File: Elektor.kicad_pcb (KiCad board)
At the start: 2 copper layers, 54 parts, among them J1 Conn_Coaxial, J13 Conn_Coaxial, J6 Conn_01x03_Pin, J7 Conn_01x02, J8 Conn_01x02, Q1 BF545B, U1 Si5351A-B-GT, U2 74HC74, U3 74HC4066D_653, U5 MCP6022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

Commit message: routage plus compact
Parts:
- removed J7: Conn_01x02, Connector_PinHeader_2.54mm:PinHeader_1x02_P2.54mm_Vertical
- added C14: 4.7u, Capacitor_THT:C_Rect_L4.0mm_W2.5mm_P2.50mm, F.Cu at (175.5, 64.5)
- added C8: 4.7u, Capacitor_THT:C_Rect_L4.0mm_W2.5mm_P2.50mm, F.Cu at (170.1, 66.0)
- R19: moved to B.Cu
- U2: value 74HC74 -> 74HC04; footprint Package_SO:SO-14_5.3x10.2mm_P1.27mm -> Package_SO:SOIC-14_3.9x8.7mm_P1.27mm
- moved R10 33.7 mm to (186.9, 68.3), turned to 90 degrees
- moved R12 33.2 mm to (183.6, 63.0), turned to 180 degrees
- moved C15 31.3 mm to (178.8, 68.8), turned to -90 degrees
- moved C3 28.4 mm to (184.9, 75.2)
- moved C4 27.5 mm to (185.2, 77.7), turned to 180 degrees
- moved R11 27.2 mm to (187.0, 63.0), turned to 180 degrees
- moved U5 26.3 mm to (182.9, 68.6), turned to 90 degrees
- moved J6 26.1 mm to (170.7, 97.0), turned to 0 degrees
- moved R9 25.8 mm to (186.9, 75.2)
- moved C6 25.4 mm to (180.8, 75.2), turned to 90 degrees
- moved Y1 24.4 mm to (166.1, 98.7), turned to 90 degrees
- moved C17 23.2 mm to (192.0, 68.6), turned to -90 degrees
- moved R3 23.2 mm to (174.8, 99.6), turned to 90 degrees
- moved R13 22.9 mm to (182.9, 75.2)
- moved C5 22.7 mm to (181.6, 77.7), turned to 180 degrees
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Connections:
- C15 pad 1: Net-(U2A-~{R}) -> 5VA
- C15 pad 2: GND -> GNDA
- C16 pad 1: Net-(U2A-~{R}) -> Net-(U2G-VCC)
- R12 pad 2: Net-(R12-Pad2) -> Net-(C8-Pad1)
- R17 pad 2: Net-(R17-Pad2) -> Net-(C14-Pad1)
- R5 pad 1: Net-(U2A-~{R}) -> Net-(U2G-VCC)
- U1 pad 10: Net-(J7-Pin_1) -> Net-(U1-CLK0)
- U2 pad 1: Net-(U2A-~{R}) -> Net-(U1-CLK0)
- U2 pad 10: Net-(U2A-~{R}) -> unconnected-(U2-Pad10)
- U2 pad 11: Net-(U1-CLK1) -> Net-(U2G-VCC)
- U2 pad 12: Net-(U2A-~{Q}) -> unconnected-(U2-Pad12)
- U2 pad 13: Net-(U2A-~{R}) -> Net-(U2G-VCC)
- U2 pad 14: Net-(U2A-~{R}) -> Net-(U2G-VCC)
- U2 pad 2: Net-(U2A-D) -> Net-(U3-1E)
- U2 pad 4: Net-(U2A-~{R}) -> Net-(U3-4E)
- U2 pad 5: Net-(U2A-Q) -> Net-(U2G-VCC)
- U2 pad 6: Net-(U2A-~{Q}) -> unconnected-(U2-Pad6)
- U2 pad 8: Net-(U2B-~{Q}) -> unconnected-(U2-Pad8)
- U2 pad 9: Net-(U2A-D) -> Net-(U2G-VCC)
- U3 pad 12: Net-(U2A-~{Q}) -> Net-(U3-4E)
- U3 pad 13: Net-(U2B-~{Q}) -> Net-(U3-1E)
- U3 pad 14: Net-(U2A-~{R}) -> Net-(U2G-VCC)
- U3 pad 5: Net-(U2A-D) -> Net-(U1-CLK0)
- U3 pad 6: Net-(U2A-Q) -> Net-(U1-CLK1)
- U5 pad 7: Net-(R12-Pad2) -> Net-(C8-Pad1)
- U6 pad 5V: Net-(U2A-~{R}) -> Net-(U2G-VCC)
- U6 pad INL: Net-(R12-Pad2) -> Net-(C8-Pad2)
- U6 pad INR: Net-(R17-Pad2) -> Net-(C14-Pad2)
- U7 pad 7: Net-(R17-Pad2) -> Net-(C14-Pad1)
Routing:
- net Net-(U2A-~{R}): track 89.3 -> 0.00 mm, vias 6 -> 0
- net GND: track 174.0 -> 115.5 mm, vias 9 -> 8
- net Net-(U3-2Z): track 64.6 -> 16.4 mm, vias 4 -> 2
- net Net-(U2A-D): track 47.2 -> 0.00 mm, vias 4 -> 0
- net Net-(U2G-VCC): track 0.00 -> 42.6 mm, vias 0 -> 2
- net Net-(U2A-~{Q}): track 40.8 -> 0.00 mm, vias 4 -> 0
- net Net-(U3-1Z): track 56.7 -> 20.1 mm, vias 4 -> 2
- net Net-(U2B-~{Q}): track 33.2 -> 0.00 mm, vias 2 -> 0
- net Net-(U2A-Q): track 27.2 -> 0.00 mm, vias 5 -> 0
- net Net-(C14-Pad1): track 0.00 -> 26.6 mm, vias 0 -> 3
- net Net-(U1-CLK0): track 0.00 -> 26.5 mm, vias 0 -> 2
- net Net-(R12-Pad2): track 25.5 -> 0.00 mm, vias 2 -> 0
- net Net-(U3-4E): track 0.00 -> 21.2 mm
- net Net-(U3-1E): track 0.00 -> 20.6 mm
- net Net-(J6-Pin_3): track 4.88 -> 25.0 mm
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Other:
- board outline added: 53 x 44 mm

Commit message: avec plan de masse
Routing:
- net GND: track 115.5 -> 136.0 mm, vias 8 -> 11
- net Net-(U3-4E): track 21.2 -> 19.7 mm
- net Net-(U6-SCL): vias 3 -> 2
- net 3.3V: vias 11 -> 10
- added copper zone on B.Cu, net GND
- added copper zone on B.Cu, net GNDA
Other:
- board size 53 x 44 mm -> 53 x 44.1 mm

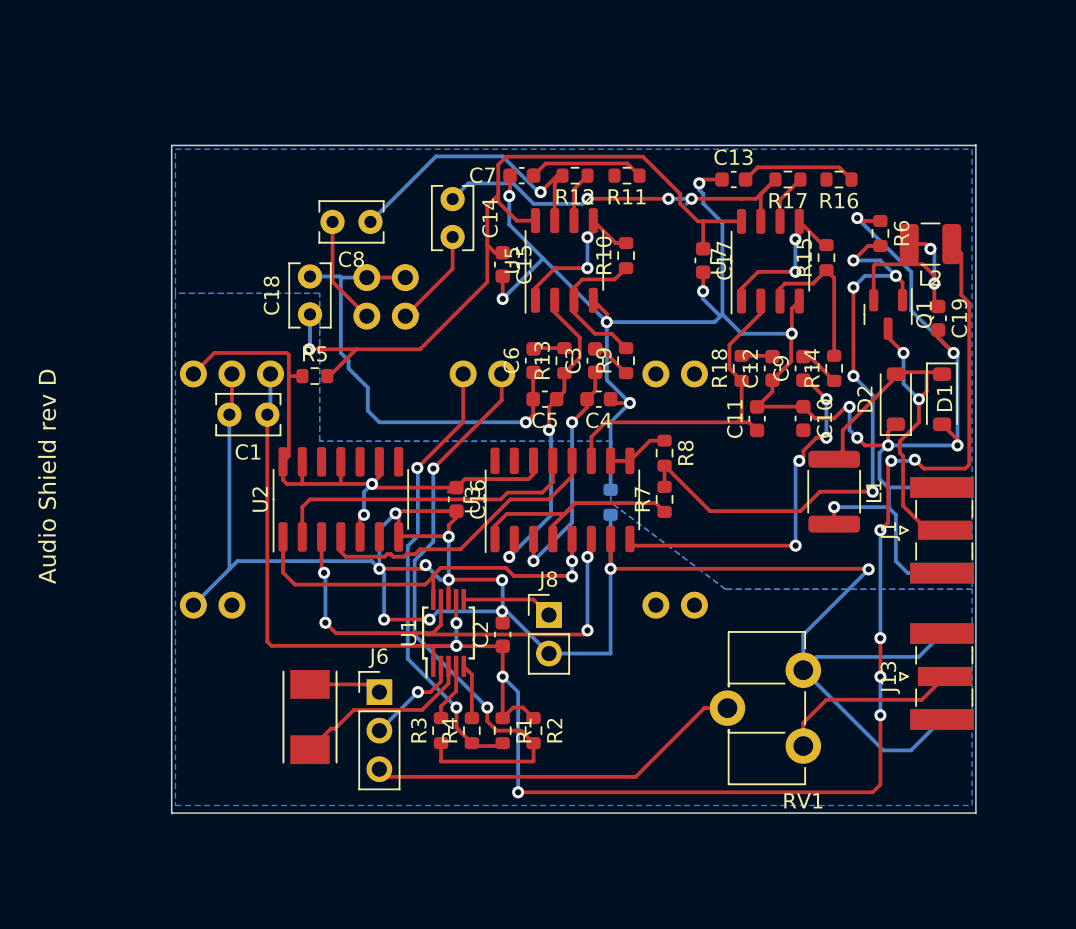
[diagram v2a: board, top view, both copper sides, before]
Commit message: meilleur plan de masse
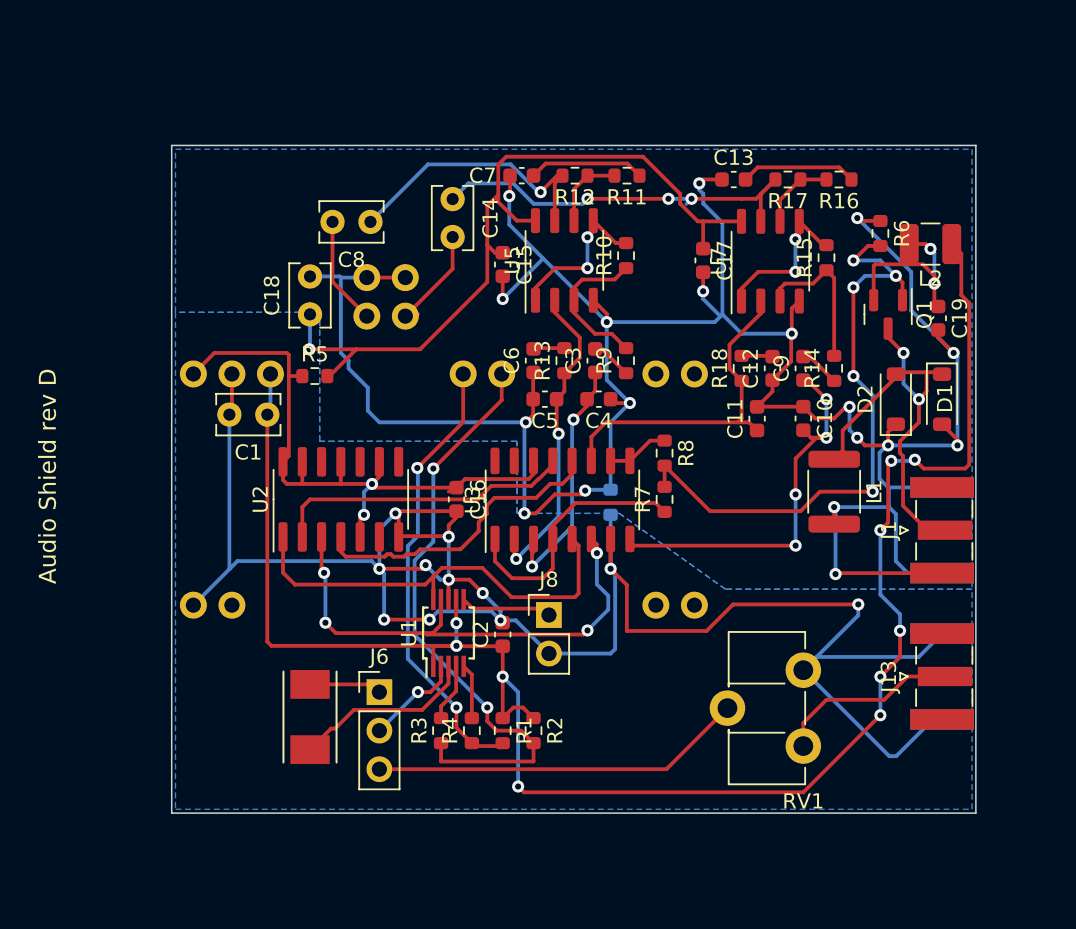
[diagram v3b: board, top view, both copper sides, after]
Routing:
- net GNDA: track 161.5 -> 183.6 mm, vias 15 -> 18
- net Net-(U1-CLK0): track 26.5 -> 28.8 mm, vias 2 -> 0
- net 3.3V: track 121.6 -> 119.7 mm
- net Net-(U5B--): track 3.33 -> 5.11 mm
- net Net-(U3-3Y): track 24.1 -> 25.9 mm
- net Net-(U7B--): track 3.31 -> 5.03 mm
- net Net-(U3-2Z): track 16.4 -> 18.0 mm
- net Net-(U3-1Y): track 15.6 -> 17.1 mm
- net Net-(U3-1Z): track 19.6 -> 20.9 mm
- net Net-(U1-CLK1): track 32.5 -> 33.4 mm
- net Net-(U3-1E): track 20.6 -> 19.9 mm
- net Net-(U3-4E): track 19.7 -> 20.3 mm
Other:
- board size 53 x 44.1 mm -> 53 x 44 mm

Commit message: plus compact
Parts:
- moved R1 22.7 mm to (169.9, 78.7), turned to 90 degrees
- moved R2 22.1 mm to (173.8, 78.7), turned to 90 degrees
- moved R6 22.0 mm to (193.0, 86.1), turned to 90 degrees
- moved L2 21.6 mm to (199.5, 87.8), turned to 90 degrees
- moved R4 21.4 mm to (171.8, 78.8), turned to -90 degrees
- moved Re 20.6 mm to (175.5, 79.0), turned to -90 degrees
- moved C19 19.3 mm to (195.5, 87.5), turned to 180 degrees
- moved Q1 14.5 mm to (195.8, 83.9), turned to 90 degrees
- moved J8 12.0 mm to (172.5, 99.5), turned to 90 degrees
- moved J1 9.52 mm to (205.0, 77.2)
- moved D1 8.47 mm to (205.8, 69.5), turned to 90 degrees
- moved D2 8.40 mm to (203.0, 69.5), turned to -90 degrees
- moved RV1 8.31 mm to (193.2, 94.2), turned to -90 degrees
- moved Y1 6.40 mm to (170.8, 94.2), turned to -90 degrees
- moved J6 5.64 mm to (166.5, 93.2)
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- renumbered R3 to Re
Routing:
- net GND: track 136.2 -> 96.6 mm, vias 11 -> 6
- net 3.3V: track 119.7 -> 84.4 mm, vias 10 -> 1
- net Net-(Q1-S): track 41.5 -> 7.59 mm, vias 5 -> 0
- net Net-(U6-SDA): track 39.4 -> 6.01 mm, vias 2 -> 0
- net Net-(U6-SCL): track 30.6 -> 7.89 mm, vias 2 -> 0
- net Net-(U3-3Y): track 25.9 -> 7.55 mm, vias 4 -> 2
- net Net-(U1-SDA): track 3.63 -> 13.4 mm, vias 0 -> 2
- net Net-(U1-SCL): track 3.82 -> 13.6 mm, vias 0 -> 2
- net Net-(Q1-D): track 13.2 -> 6.21 mm, vias 2 -> 0
- net Net-(U1-XB): track 12.9 -> 6.56 mm
- net GNDA: track 183.6 -> 177.8 mm, vias 18 -> 13
- net Net-(J6-Pin_3): track 24.6 -> 30.4 mm, vias 0 -> 1
- net Net-(J6-Pin_2): track 6.40 -> 11.0 mm, vias 1 -> 0
- net Net-(D1-K): track 29.0 -> 25.4 mm, vias 2 -> 0
- net Net-(U1-CLK0): track 28.8 -> 31.9 mm, vias 0 -> 4
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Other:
- board size 53 x 44 mm -> 50 x 44 mm

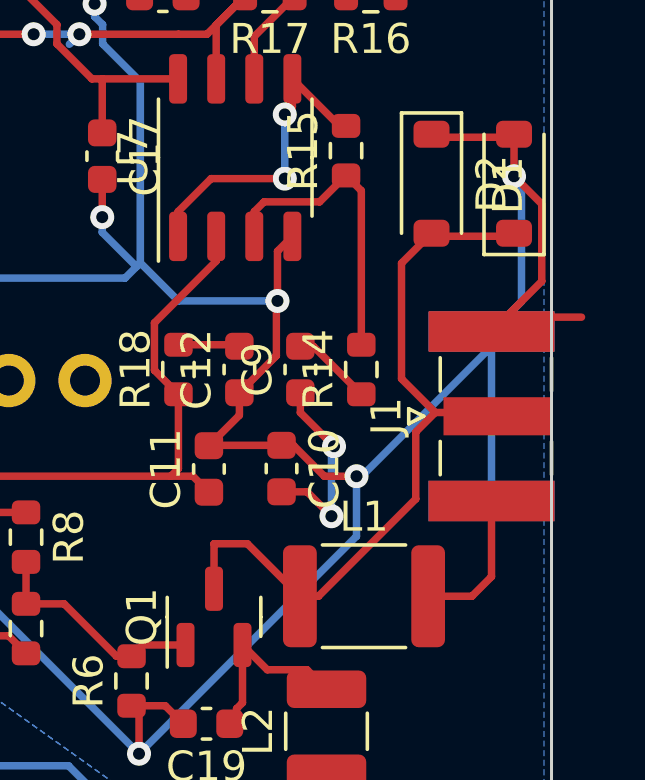
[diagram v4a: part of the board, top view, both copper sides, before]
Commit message: ajout connexion manquante
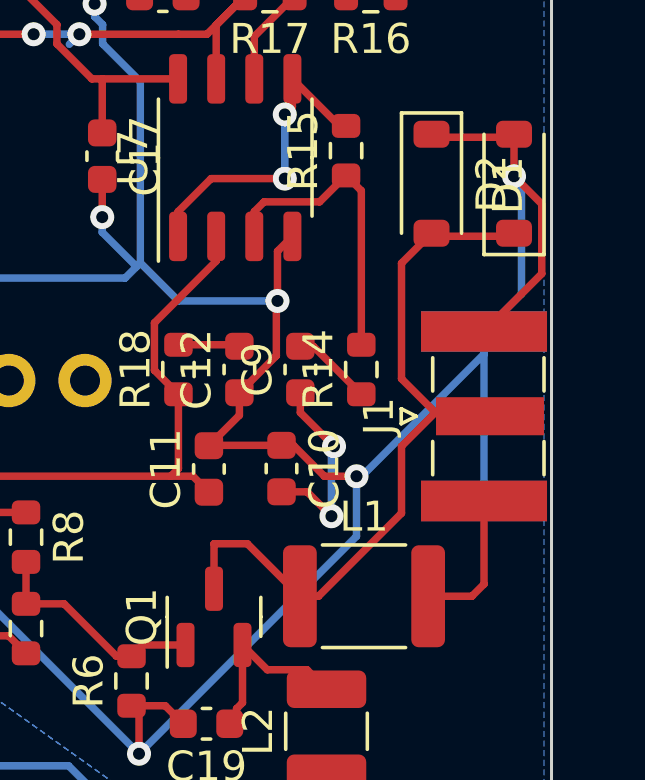
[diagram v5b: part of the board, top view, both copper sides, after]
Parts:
- moved J1 0.25 mm to (204.8, 77.2)
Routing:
- net GNDA: track 177.8 -> 175.5 mm

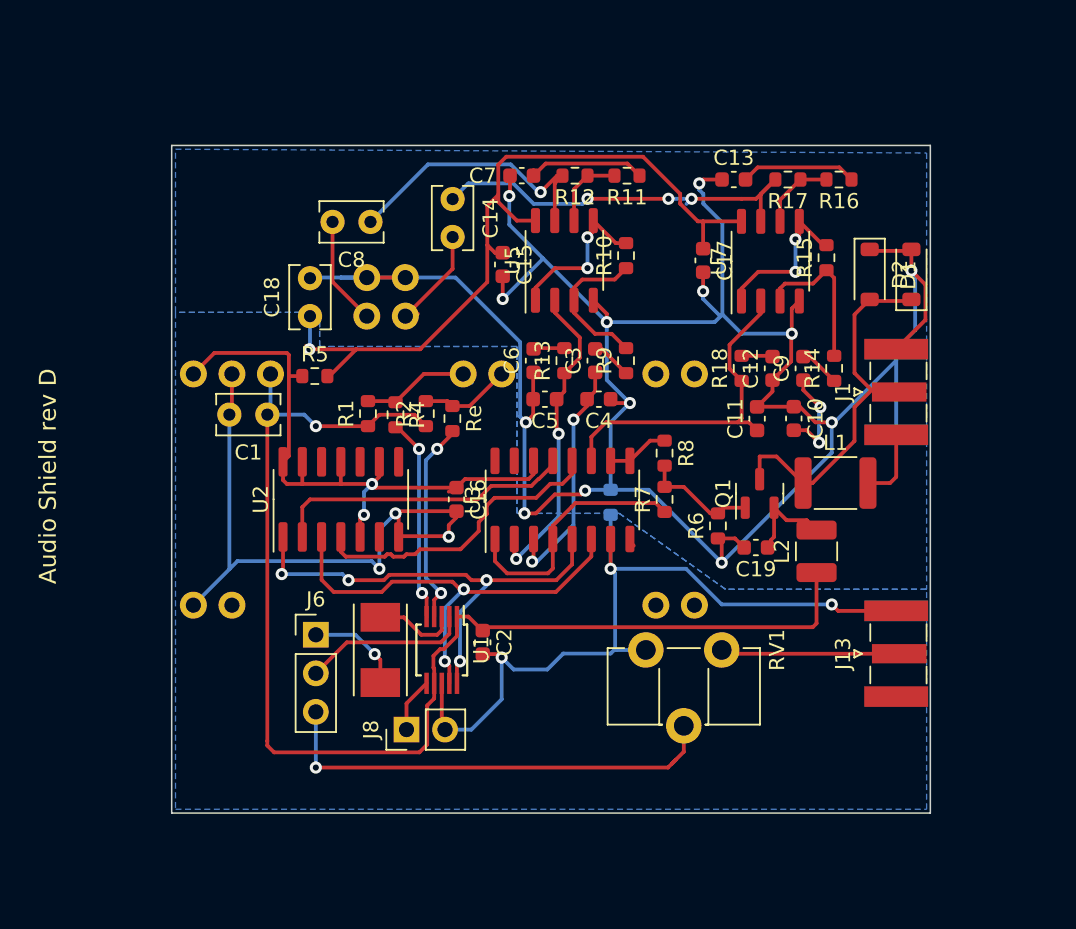
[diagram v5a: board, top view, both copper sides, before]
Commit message: 4066 avait 16 broches au lieu de 14 !
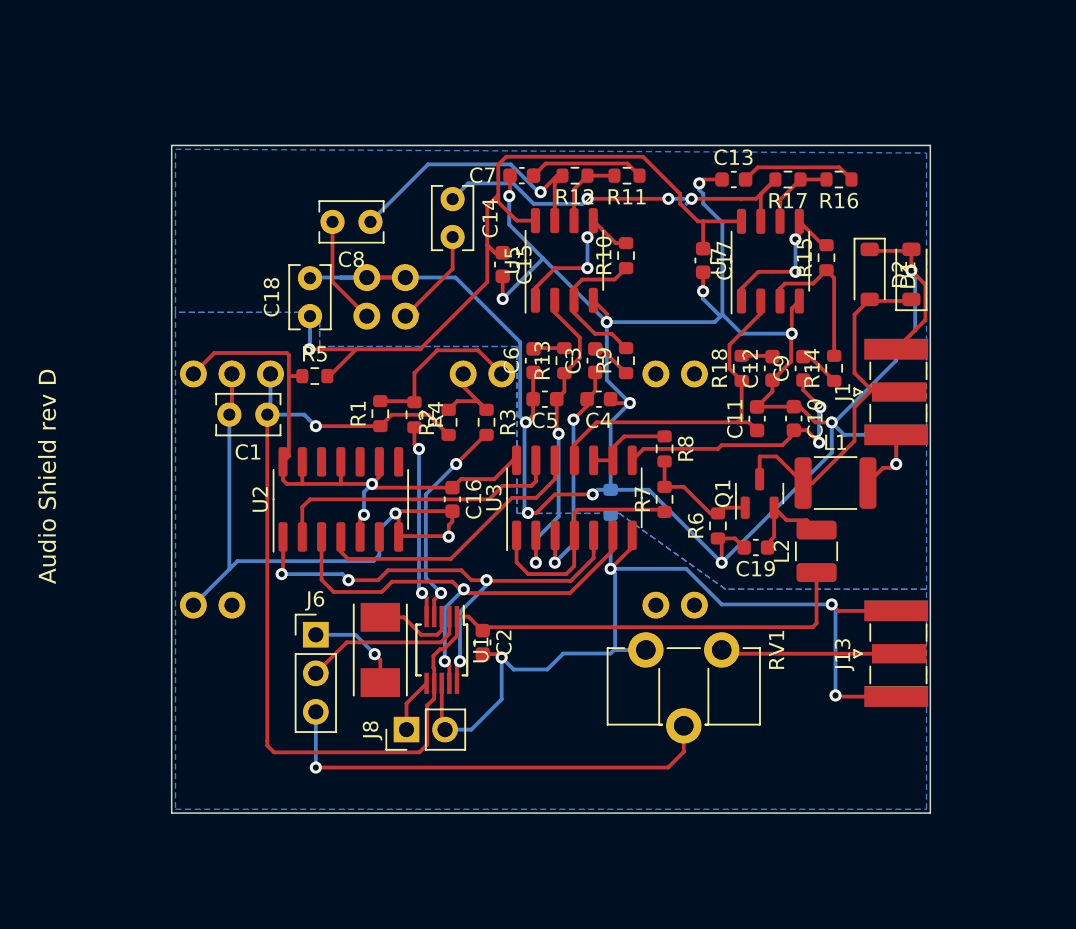
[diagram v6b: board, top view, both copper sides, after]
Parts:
- U3: footprint Package_SO:SO-16_3.9x9.9mm_P1.27mm -> Package_SO:SOIC-14_3.9x8.7mm_P1.27mm
- moved R3 2.26 mm to (177.8, 79.2)
- moved R2 1.61 mm to (175.2, 79.2)
- moved R4 1.25 mm to (173.0, 78.8)
- moved R1 0.81 mm to (170.8, 78.7)
- moved U3 0.80 mm to (183.5, 84.2)
- moved R8 0.28 mm to (189.5, 81.0)
- moved C16 0.27 mm to (175.5, 84.3)
- renumbered Re to R3
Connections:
- R1 pad 2: Net-(U6-SCL) -> Net-(U6-SDA)
- R2 pad 2: Net-(U6-SDA) -> Net-(U6-SCL)
- R3 pad 1: Net-(U6-SDA) -> Net-(U6-SCL)
- R4 pad 1: Net-(U6-SCL) -> Net-(U6-SDA)
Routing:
- net Net-(U3-3Y): track 7.55 -> 18.6 mm
- net GND: track 96.6 -> 106.5 mm
- net Net-(U6-SDA): track 6.01 -> 11.2 mm
- net Net-(U3-3Z): track 4.11 -> 6.21 mm
- net 3.3V: track 84.4 -> 86.1 mm
- net Net-(U1-CLK0): track 31.9 -> 33.6 mm
- net Net-(U2G-VCC): track 42.6 -> 41.0 mm
- net Net-(U3-4E): track 20.3 -> 18.7 mm
- net Net-(U1-CLK1): track 30.5 -> 31.9 mm
- net Net-(U6-SCL): track 7.89 -> 6.79 mm
- net Net-(U3-1Y): track 16.8 -> 15.7 mm
- net Net-(U1-SCL): track 13.6 -> 14.3 mm
- net Net-(U1-SDA): track 13.4 -> 12.8 mm
- net GNDA: track 175.5 -> 175.8 mm, vias 13 -> 14

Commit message: release V1.1
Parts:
- removed J13: Conn_Coaxial, Connector_Coaxial:SMA_Samtec_SMA-J-P-X-ST-EM1_EdgeMount
- removed J6: Conn_01x03_Pin, Connector_PinHeader_2.54mm:PinHeader_1x03_P2.54mm_Vertical
- removed J8: Conn_01x02, Connector_PinHeader_2.54mm:PinHeader_1x02_P2.54mm_Vertical
- removed RV1: 1K, Potentiometer_THT:Potentiometer_ACP_CA9-H5_Horizontal
- added GNDA: Conn_01x01_Pin, Library_test_point:Test_point_jose_D1.8mm_Drill1.0mm, F.Cu at (162.6, 70.4)
- added GNDD: Conn_01x01_Pin, Library_test_point:Test_point_jose_D1.8mm_Drill1.0mm, F.Cu at (190.5, 94.5)
- added R20: 1K, Resistor_SMD:R_0603_1608Metric, F.Cu at (165.9, 66.9)
- added R21: 1K, Resistor_SMD:R_0603_1608Metric, F.Cu at (175.5, 70.4)
- added R22: 10K, Resistor_SMD:R_0402_1005Metric, F.Cu at (181.3, 93.6)
- added TP2: Conn_01x01_Pin, Library_test_point:Test_point_jose_D1.8mm_Drill1.0mm, F.Cu at (168.3, 63.9)
- added TP3: Conn_01x01_Pin, Library_test_point:Test_point_jose_D1.8mm_Drill1.0mm, F.Cu at (173.0, 67.1)
- added TP4: Conn_01x01_Pin, Library_test_point:Test_point_jose_D1.8mm_Drill1.0mm, F.Cu at (162.1, 84.6)
- added TP5: Conn_01x01_Pin, Library_test_point:Test_point_jose_D1.8mm_Drill1.0mm, F.Cu at (167.1, 93.5)
- added TP6: Conn_01x01_Pin, Library_test_point:Test_point_jose_D1.8mm_Drill1.0mm, F.Cu at (184.2, 94.5)
- added TP7: Conn_01x01_Pin, Library_test_point:Test_point_jose_D1.8mm_Drill1.0mm, F.Cu at (178.8, 71.9)
- added TP8: Conn_01x01_Pin, Library_test_point:Test_point_jose_D1.8mm_Drill1.0mm, F.Cu at (190.5, 71.9)
- moved R16 2.36 mm to (198.6, 63.5)
- moved R17 2.30 mm to (195.3, 63.5)
- moved C13 2.04 mm to (192.0, 63.5)
- moved C8 1.00 mm to (170.6, 66.9)
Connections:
- net 5VA renamed 3.3VA
- C14 pad 2: Net-(C14-Pad2) -> Net-(TP3-Pin_1)
- C8 pad 2: Net-(C8-Pad2) -> Net-(TP2-Pin_1)
- R10 pad 1: Net-(U5A-+) -> Net-(U5A--)
- R14 pad 2: Net-(U7A-+) -> Net-(U7A--)
- R15 pad 1: Net-(U7A-+) -> Net-(U7A--)
- R19 pad 1: GND -> unconnected-(R19-Pad1)
- R5 pad 1: Net-(U2G-VCC) -> 3.3V
- R9 pad 2: Net-(U5A-+) -> Net-(U5A--)
- U1 pad 2: Net-(J6-Pin_2) -> Net-(U1-XA)
- U5 pad 2: Net-(U3-1Z) -> Net-(U5A--)
- U5 pad 3: Net-(U5A-+) -> Net-(U3-1Z)
- U6 pad INL: Net-(C8-Pad2) -> Net-(R20-Pad1)
- U6 pad INR: Net-(C14-Pad2) -> Net-(R21-Pad1)
- U7 pad 2: Net-(U3-4Y) -> Net-(U7A--)
- U7 pad 3: Net-(U7A-+) -> Net-(U3-4Y)
- Y1 pad 2: Net-(J6-Pin_1) -> Net-(U1-XA)
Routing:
- net Net-(J6-Pin_3): track 30.1 -> 0.00 mm, vias 1 -> 0
- net GND: track 106.5 -> 79.9 mm, vias 6 -> 4
- net Net-(Q1-S): track 7.87 -> 27.1 mm
- net Net-(J13-In): track 12.9 -> 0.00 mm
- net Net-(U7A--): track 0.00 -> 11.3 mm
- net Net-(U5A--): track 0.00 -> 11.3 mm
- net Net-(J6-Pin_2): track 11.0 -> 0.00 mm
- net Net-(U7A-+): track 10.2 -> 0.00 mm
- net Net-(U5A-+): track 10.0 -> 0.00 mm
- net Net-(U1-CLK2): track 3.60 -> 12.1 mm
- net Net-(C14-Pad2): track 7.40 -> 0.00 mm
- net Net-(R20-Pad1): track 0.00 -> 7.36 mm
- net Net-(C8-Pad2): track 7.33 -> 0.00 mm
- net Net-(U1-XA): track 0.00 -> 6.96 mm
- net Net-(J6-Pin_1): track 6.44 -> 0.00 mm, vias 1 -> 0
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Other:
- board size 50 x 44 mm -> 50 x 42 mm
- board text added: "4066"
- board text added: "7404"
- board text added: "SDR TEENSY V1.1 F1FGV F1VL"
- board text added: "Teensy USB side"
